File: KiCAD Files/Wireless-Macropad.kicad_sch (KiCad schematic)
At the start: 22 parts, among them SW1 RotaryEncoder_Switch, SW10 SW_SPDT, SW2 SW_Push, SW3 SW_Push, SW4 SW_Push, SW5 SW_Push, SW6 SW_Push, SW7 SW_Push, SW8 SW_Push, SW9 SW_Push, U1 106990290

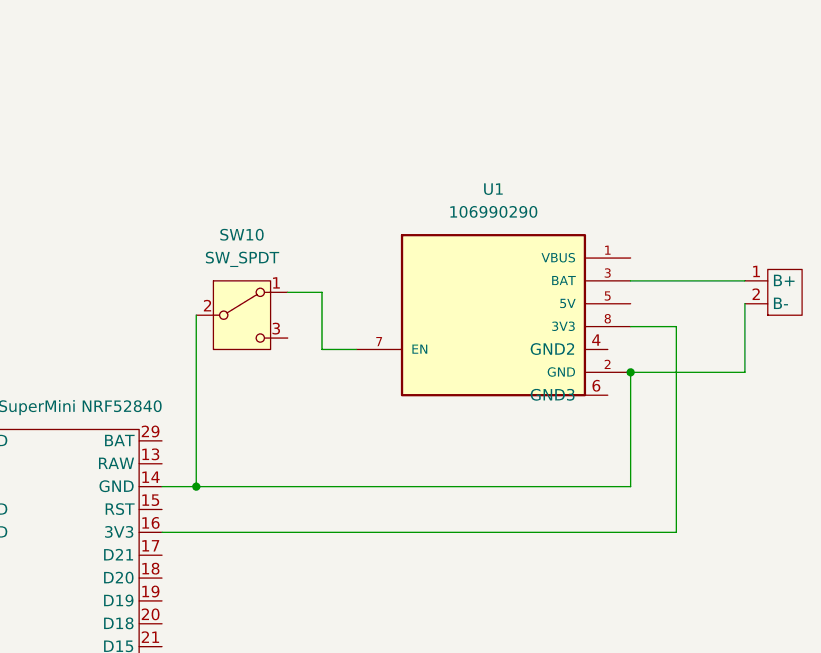
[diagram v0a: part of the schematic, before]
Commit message: Updated my PCB and generated my gerber file
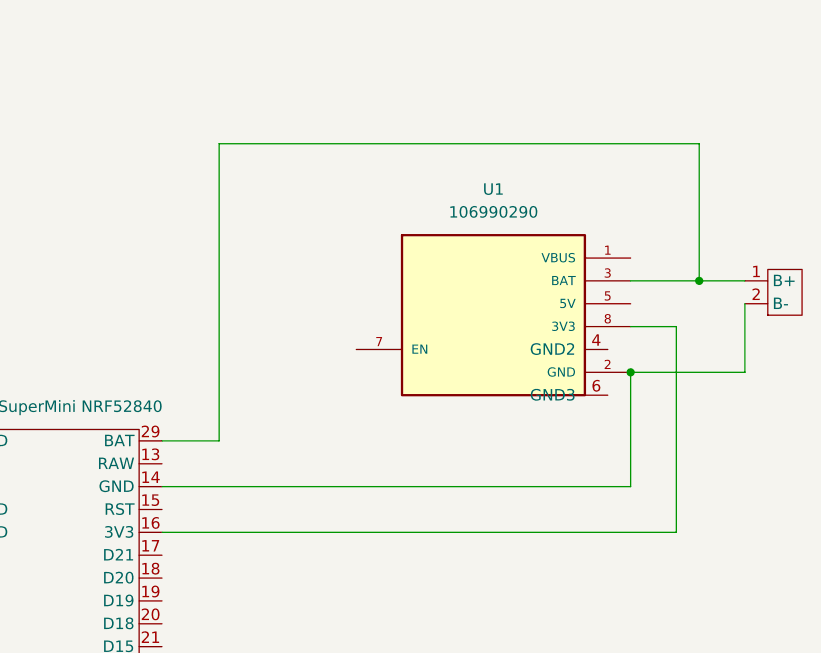
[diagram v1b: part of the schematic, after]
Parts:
- removed SW10: SW_SPDT, Button_Switch_SMD:SW_SPDT_CK_JS102011SAQN, symbol Switch:SW_SPDT
- U3: footprint Connector_JST:JST_PH_B2B-PH-K_1x02_P2.00mm_Vertical -> Connector_JST:JST_PH_S2B-PH-K_1x02_P2.00mm_Horizontal
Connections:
- net at U1.3 (BAT), U3.1 (B+): now also U2.29 (BAT)
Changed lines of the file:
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@@
+	)
+	(junction
+		(at 228.6 53.34)
+		(diameter 0)
+		(color 0 0 0 0)
 	)
 	(junction
@@
 		(color 0 0 0 0)
 	)
-	(junction
-		(at 172.72 76.2)
-		(diameter 0)
-		(color 0 0 0 0)
-	)
 	(wire
 		(pts
@@
 	(wire
 		(pts
-			(xy 168.91 76.2) (xy 172.72 76.2)
+			(xy 168.91 76.2) (xy 220.98 76.2)
 		)
 		(stroke
@@
 	(wire
 		(pts
+			(xy 228.6 38.1) (xy 175.26 38.1)
+		)
+		(stroke
+			(width 0)
+			(type default)
+		)
+	)
+	(wire
+		(pts
 			(xy 139.7 86.36) (xy 144.78 86.36)
 		)
@@
 	(wire
 		(pts
-			(xy 172.72 76.2) (xy 220.98 76.2)
+			(xy 228.6 53.34) (xy 233.68 53.34)
 		)
 		(stroke
@@
 	(wire
 		(pts
-			(xy 190.5 60.96) (xy 186.69 60.96)
-		)
-		(stroke
-			(width 0)
-			(type default)
-		)
-	)
-	(wire
-		(pts
 			(xy 85.09 43.18) (xy 85.09 58.42)
 		)
@@
 	(wire
 		(pts
-			(xy 186.69 54.61) (xy 182.88 54.61)
-		)
-		(stroke
-			(width 0)
-			(type default)
-		)
-	)
-	(wire
-		(pts
-			(xy 220.98 53.34) (xy 233.68 53.34)
+			(xy 220.98 53.34) (xy 228.6 53.34)
 		)
 		(stroke
@@
 	(wire
 		(pts
-			(xy 172.72 57.15) (xy 172.72 76.2)
-		)
-		(stroke
-			(width 0)
-			(type default)
-		)
-	)
-	(wire
-		(pts
 			(xy 63.5 76.2) (xy 64.77 76.2)
 		)
@@
 	(wire
 		(pts
+			(xy 175.26 71.12) (xy 168.91 71.12)
+		)
+		(stroke
+			(width 0)
+			(type default)
+		)
+	)
+	(wire
+		(pts
 			(xy 139.7 91.44) (xy 144.78 91.44)
 		)
@@
 	(wire
 		(pts
-			(xy 186.69 60.96) (xy 186.69 54.61)
-		)
-		(stroke
-			(width 0)
-			(type default)
-		)
-	)
-	(wire
-		(pts
 			(xy 144.78 71.12) (xy 144.78 26.67)
 		)
@@
 	(wire
 		(pts
+			(xy 228.6 53.34) (xy 228.6 38.1)
+		)
+		(stroke
+			(width 0)
+			(type default)
+		)
+	)
+	(wire
+		(pts
 			(xy 64.77 54.61) (xy 90.17 54.61)
 		)
@@
 		(pts
 			(xy 62.23 43.18) (xy 59.69 43.18)
+		)
+		(stroke
+			(width 0)
+			(type default)
+		)
+	)
+	(wire
+		(pts
+			(xy 175.26 38.1) (xy 175.26 71.12)
 		)
 		(stroke
@@
 			)
 		)
-		(property "Footprint" "Connector_JST:JST_PH_B2B-PH-K_1x02_P2.00mm_Vertical"
+		(property "Footprint" "Connector_JST:JST_PH_S2B-PH-K_1x02_P2.00mm_Horizontal"
 			(at 236.22 54.61 0)
 			(effects
@@
 					(unit 1)
 				)
-			)
-		)
-	)
-	(symbol
-		(lib_id "Switch:SW_SPDT")
-		(at 177.8 57.15 0)
-		(unit 1)
-		(exclude_from_sim no)
-		(in_bom yes)
-		(on_board yes)
-		(dnp no)
-		(fields_autoplaced yes)
-		(property "Reference" "SW10"
-			(at 177.8 48.26 0)
-			(effects
-				(font
-					(size 1.27 1.27)
-				)
-			)
-		)
-		(property "Value" "SW_SPDT"
-			(at 177.8 50.8 0)
-			(effects
-				(font
-					(size 1.27 1.27)
-				)
-			)
-		)
-		(property "Footprint" "Button_Switch_SMD:SW_SPDT_CK_JS102011SAQN"
-			(at 177.8 57.15 0)
-			(effects
-				(font
-					(size 1.27 1.27)
-				)
-				(hide yes)
-			)
-		)
-		(property "Datasheet" "~"
-			(at 177.8 64.77 0)
-			(effects
-				(font
-					(size 1.27 1.27)
-				)
-				(hide yes)
-			)
-		)
-		(property "Description" "Switch, single pole double throw"
-			(at 177.8 57.15 0)
-			(effects
-				(font
-					(size 1.27 1.27)
-				)
-				(hide yes)
-			)
-		)
-		(pin "3"
-		)
-		(pin "1"
-		)
-		(pin "2"
-		)
-		(instances
-			(project ""
-				(path "/5d689967-24e5-461c-a95a-a728a90ffbb3"
-					(reference "SW10")
-					(unit 1)
-				)
